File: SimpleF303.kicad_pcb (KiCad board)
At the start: 2 copper layers, 39.7 x 61.7 mm, 28 parts, among them J1 47346-0001, J2 Conn_01x20_Male, J3 Conn_01x20_Male, SW1 B3U-1000P, U1 AZ1117CH-3.3TRG1, U2 STM32F303CCT6, Y1 8Mhz 20pf

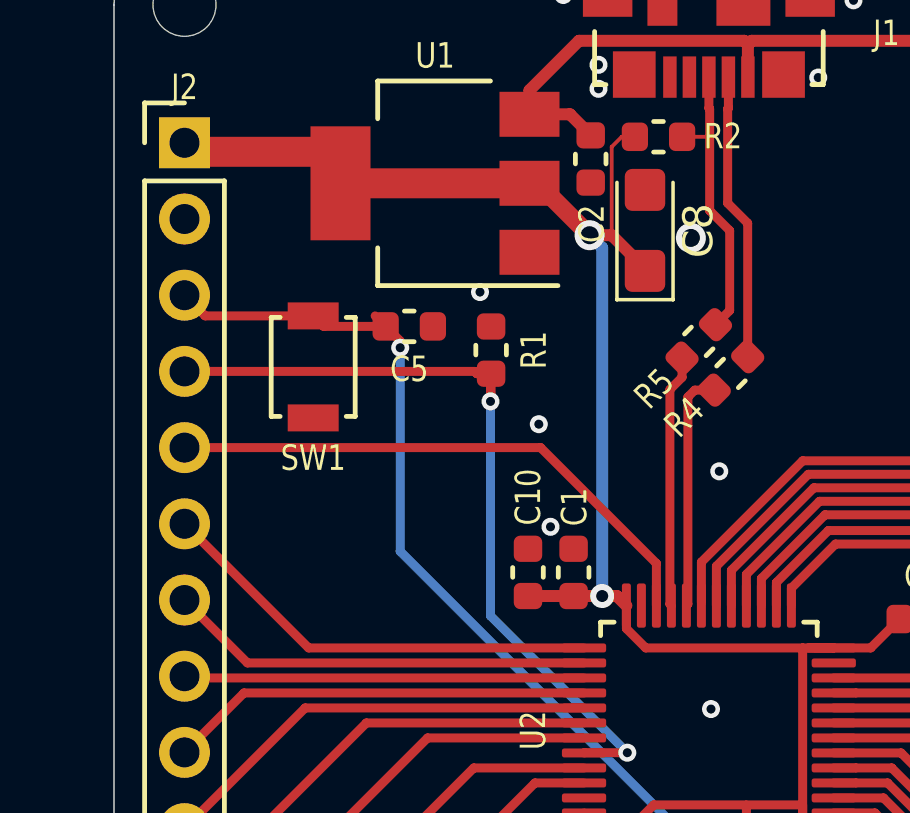
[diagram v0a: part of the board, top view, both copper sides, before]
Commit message: clearly I can't get some parts so I change selection
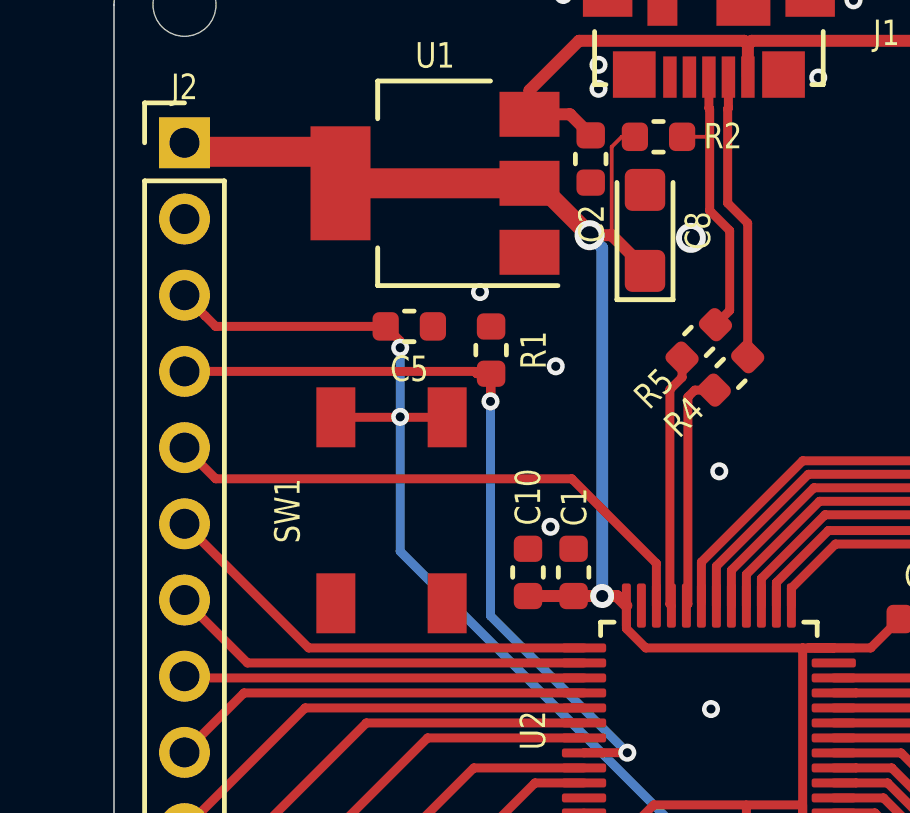
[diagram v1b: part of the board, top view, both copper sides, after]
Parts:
- SW1: footprint Button_Switch_SMD:SW_SPST_B3U-1000P -> KiCad:K2-1187SQ-A4SW-06
- moved SW1 5.45 mm to (117.8, 131.8)
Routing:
- net /NRST: track 30.7 -> 33.9 mm, vias 2 -> 3

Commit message: small changes
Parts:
- SW1: value B3U-1000P -> K2-1187SQ-A4SW-06
- moved SW1 23.8 mm to (138.8, 120.5), turned to 0 degrees
- moved C5 21.0 mm to (139.4, 124.5)
- moved R1 7.72 mm to (113.8, 123.9)
- moved C8 6.33 mm to (120.8, 125.7), turned to 0 degrees
- moved C4 5.89 mm to (128.0, 153.1), turned to 90 degrees
- moved C3 2.58 mm to (124.6, 153.1), turned to 90 degrees
- moved C6 2.13 mm to (121.8, 144.6), turned to 180 degrees
- moved C12 2.11 mm to (133.8, 145.7), turned to 270 degrees
- moved C11 1.52 mm to (132.3, 145.7), turned to 270 degrees
- moved C7 1.45 mm to (121.8, 143.1), turned to 180 degrees
- moved R3 1.14 mm to (128.2, 146.6), turned to 180 degrees
- moved Y1 0.58 mm to (127.1, 149.4), turned to 270 degrees
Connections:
- J2 pad 10: /PB5 -> /PB6
- J2 pad 11: /PB6 -> /PB7
- J2 pad 12: /PB7 -> /PB8
- J2 pad 13: /PB8 -> /PB9
- J2 pad 14: /PB9 -> /PC13
- J2 pad 15: /PC13 -> /PC14
- J2 pad 16: /PC14 -> /PC15
- J2 pad 17: /PC15 -> /PA0
- J2 pad 18: /PA0 -> /PA1
- J2 pad 19: /PA1 -> /PA2
- J2 pad 3: /NRST -> /BOOT0
- J2 pad 4: /BOOT0 -> /PA13
- J2 pad 5: /PA13 -> /PA14
- J2 pad 6: /PA14 -> /PA15
- J2 pad 7: /PA15 -> /PB3
- J2 pad 8: /PB3 -> /PB4
- J2 pad 9: /PB4 -> /PB5
- J3 pad 10: /PB10 -> /PB11
- J3 pad 11: /PB2 -> /PB10
- J3 pad 12: /PB1 -> /PB2
- J3 pad 13: /PB0 -> /PB1
- J3 pad 14: /PA7 -> /PB0
- J3 pad 15: /PA6 -> /PA7
- J3 pad 16: /PA5 -> /PA6
- J3 pad 17: /PA4 -> /PA5
- J3 pad 18: /PA3 -> /PA4
- J3 pad 19: /PA2 -> /PA3
- J3 pad 2: /PA10 -> /NRST
- J3 pad 3: /PA9 -> /PA10
- J3 pad 4: /PA8 -> /PA9
- J3 pad 5: /PB15 -> /PA8
- J3 pad 6: /PB14 -> /PB15
- J3 pad 7: /PB13 -> /PB14
- J3 pad 8: /PB12 -> /PB13
- J3 pad 9: /PB11 -> /PB12
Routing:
- net /PA2: track 28.8 -> 36.6 mm
- net +3V3: track 71.3 -> 74.9 mm, vias 2 -> 0
- net Net-(C4-Pad2): track 3.05 -> 6.59 mm
- net /NRST: track 33.9 -> 37.0 mm, vias 3 -> 2
- net /PA3: track 27.2 -> 29.7 mm
- net /PA6: track 21.4 -> 23.8 mm
- net /PA5: track 23.3 -> 25.8 mm
- net /PA4: track 25.3 -> 27.7 mm
- net /PA7: track 19.5 -> 21.9 mm
- net /PB0: track 17.8 -> 19.9 mm
- net /PA13: track 18.7 -> 20.6 mm, vias 0 -> 1
- net /PB12: track 17.8 -> 19.2 mm
- net /PC14: track 22.4 -> 21.2 mm
- net /PC13: track 20.8 -> 19.6 mm
- net /PC15: track 24.1 -> 22.9 mm
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
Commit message: Appearently buy parts is hard
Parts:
- moved R1 12.6 mm to (119.2, 135.3), turned to 0 degrees
- moved C5 8.18 mm to (133.0, 129.6)
- moved SW1 6.03 mm to (133.8, 124.0), turned to 270 degrees
- moved C2 4.40 mm to (120.6, 117.9), turned to 0 degrees
- moved U1 3.61 mm to (122.2, 123.0), turned to 270 degrees
- moved C8 3.55 mm to (120.8, 129.2), turned to 180 degrees
- moved R2 3.37 mm to (127.5, 122.6), turned to 270 degrees
- moved C1 2.15 mm to (123.7, 131.7), turned to 180 degrees
- moved C10 1.48 mm to (123.7, 133.2), turned to 180 degrees
- moved J1 0.65 mm to (128.4, 115.2)
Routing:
- net +5V: track 30.7 -> 42.7 mm
- net /USB_D+: track 9.66 -> 12.7 mm
- net /NRST: track 37.0 -> 34.3 mm
- net /USB_D-: track 9.61 -> 10.5 mm
- net /BOOT0: track 26.7 -> 25.9 mm
- net +3V3: track 74.9 -> 75.7 mm
- net GND: vias 189 -> 272
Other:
- board text added: "3.3V GND BOOT0 PA13 PA14 PA15 PB3 PB4 PB5 PB6 PB7 PB8 PB9 PC13 PC14 PC15 PA0 PA1 PA2 GND"
- board text added: "5V NRST PA10 PA9 PA8 PB15 PB14 PB13 PB12 PB11 PB10 PB2 PB1 PB0 PA7 PA6 PA5 PA4 PA3 GND"

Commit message: update pcb, add BOM, edit readme
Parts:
- moved SW1 2.91 mm to (136.3, 125.6), turned to 180 degrees
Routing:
- net /NRST: track 34.3 -> 33.2 mm
- net GND: vias 272 -> 13
